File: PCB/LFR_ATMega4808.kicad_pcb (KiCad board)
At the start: 2 copper layers, 51.6 x 67.2 mm, 49 parts, among them J1 Conn_02x02_Odd_Even, J2 Conn_02x05_Odd_Even, J3 Conn_02x02_Counter_Clockwise, J4 Conn_02x02_Counter_Clockwise, J5 Conn_02x02_Counter_Clockwise, J6 Conn_02x03_Odd_Even, Q2 NMOS, Q3 NMOS, U1 ATmega4808-A, U5 MCP1700x-330xxTO

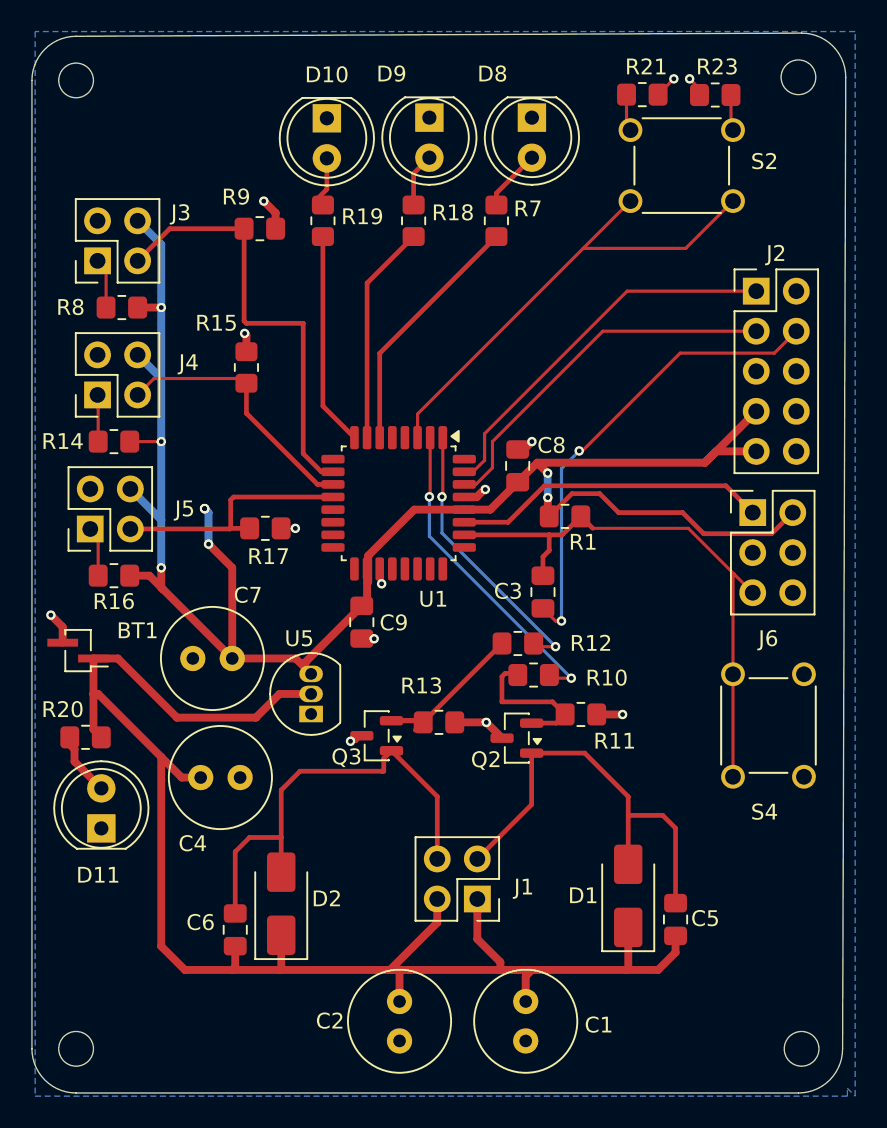
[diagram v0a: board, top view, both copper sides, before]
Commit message: Increased 4.8V track width to 1mm
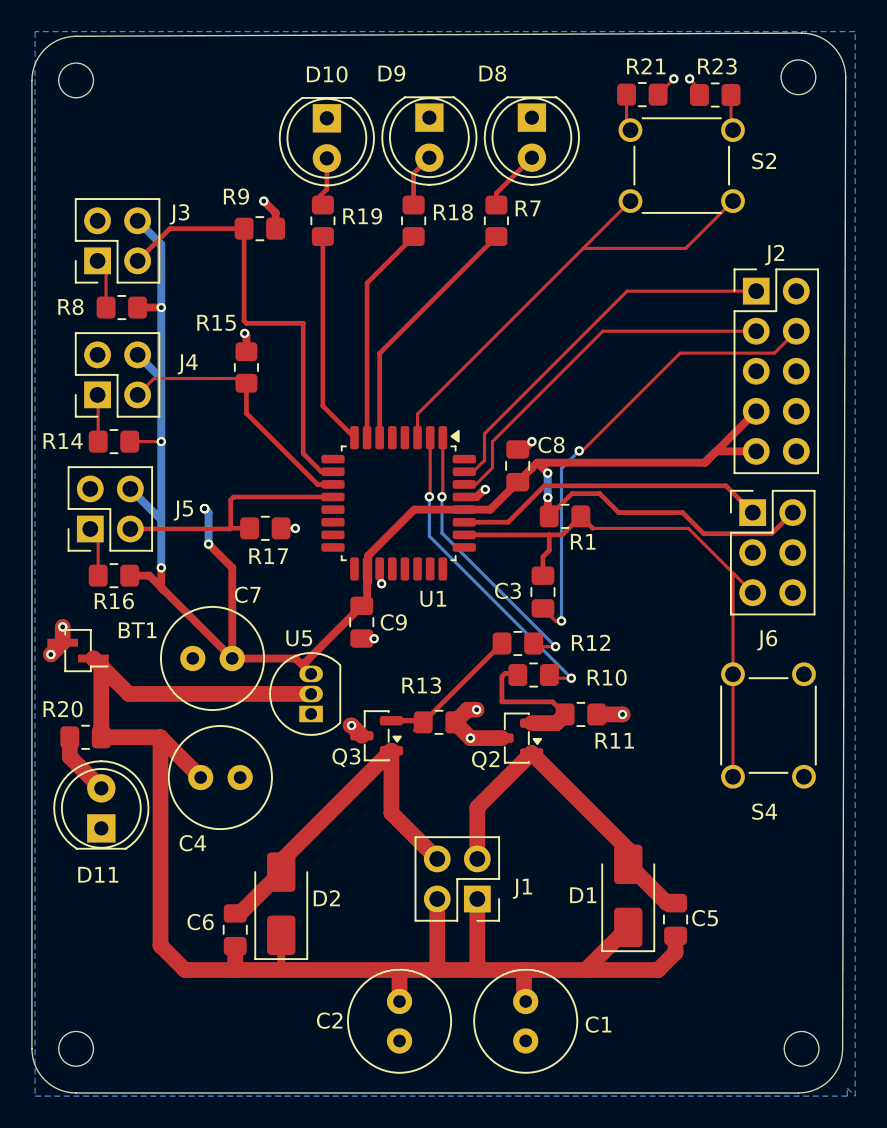
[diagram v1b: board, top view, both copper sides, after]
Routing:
- net Net-(D2-A): track 29.0 -> 22.7 mm
- net Net-(D1-A): track 27.8 -> 21.7 mm
- net +4.8V: track 98.6 -> 96.1 mm
- net GND: track 19.7 -> 21.6 mm, vias 13 -> 15

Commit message: Slight trace redesign
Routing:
- net ADC Sensor 3: track 27.9 -> 25.8 mm
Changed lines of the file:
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@@
 	)
 	(segment
-		(start 146.25 101)
-		(end 141.54 101)
+		(start 151.150001 116.4125)
+		(end 147.45 112.712499)
 		(width 0.3)
 		(layer "F.Cu")
@@
 	)
 	(segment
-		(start 150 115.262499)
-		(end 151.150001 116.4125)
+		(start 146.25 101)
+		(end 141.54 101)
 		(width 0.3)
 		(layer "F.Cu")
@@
 	)
 	(segment
-		(start 146.25 101)
-		(end 146.25 106.85)
+		(start 147.45 102.2)
+		(end 146.25 101)
 		(width 0.3)
 		(layer "F.Cu")
@@
 	)
 	(segment
-		(start 146.4 107)
-		(end 150 107)
+		(start 151.8875 116.4125)
+		(end 151.150001 116.4125)
 		(width 0.3)
 		(layer "F.Cu")
@@
 	)
 	(segment
-		(start 150 107)
-		(end 150 115.262499)
+		(start 147.45 112.712499)
+		(end 147.45 102.2)
 		(width 0.3)
 		(layer "F.Cu")
-		(net "ADC Sensor 3")
-	)
-	(segment
-		(start 146.25 106.85)
-		(end 146.4 107)
-		(width 0.3)
-		(layer "F.Cu")
-		(net "ADC Sensor 3")
-	)
-	(segment
-		(start 151.150001 116.4125)
-		(end 151.8875 116.4125)
-		(width 0.3)
-		(layer "F.Cu")
